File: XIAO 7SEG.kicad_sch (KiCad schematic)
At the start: 8 parts, among them J2 Conn_01x07, J4 Conn_01x07, Q1 AO3400A, Q2 AO3400A, U1 GS2816CW-G, U2 GS2816CW-G

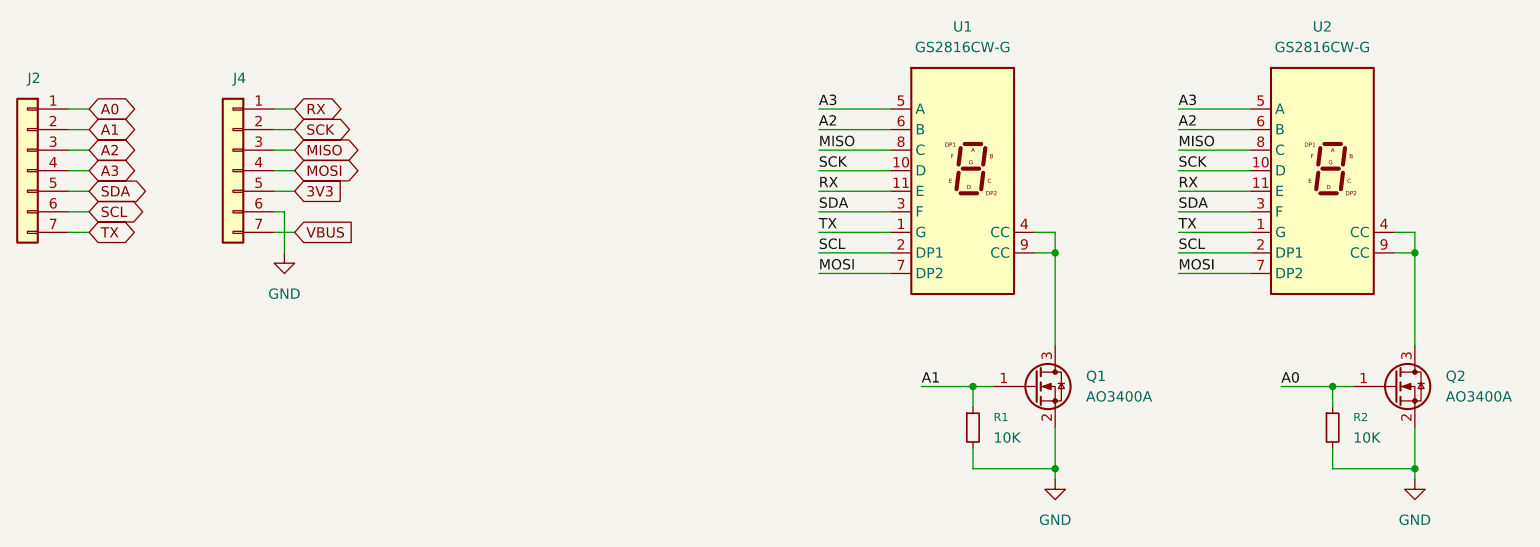
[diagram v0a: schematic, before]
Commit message: V2: Add series resistors
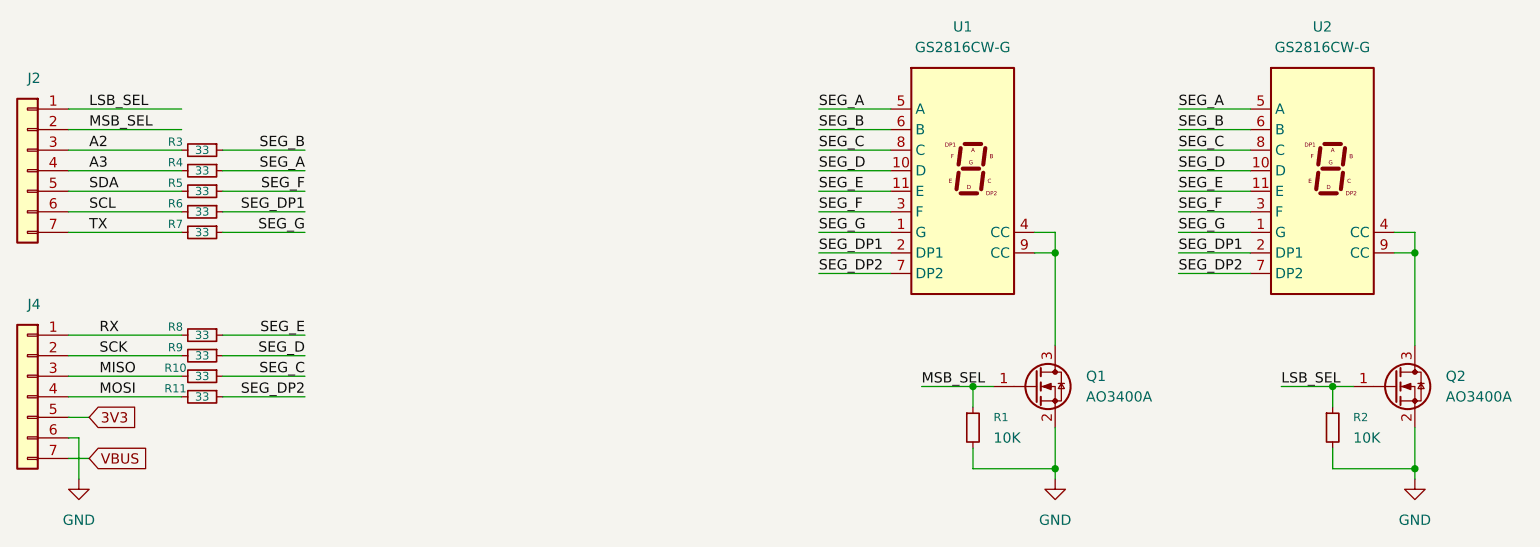
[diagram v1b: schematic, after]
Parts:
- added R10, R11, R3, R4, R5, R6, R7, R8, R9: 33, Resistor_SMD:R_0402_1005Metric, symbol Device:R_Small
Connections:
- net A2: now also R3.2; no longer U1.6 (B), U2.6 (B)
- net A3: now also R4.2; no longer U1.5 (A), U2.5 (A)
- net MISO: now also R10.2; no longer U1.8 (C), U2.8 (C)
- net MOSI: now also R11.2; no longer U1.7 (DP2), U2.7 (DP2)
- net RX: now also R8.2; no longer U1.11 (E), U2.11 (E)
- net SCK: now also R9.2; no longer U1.10 (D), U2.10 (D)
- net SCL: now also R6.2; no longer U1.2 (DP1), U2.2 (DP1)
- net SDA: now also R5.2; no longer U1.3 (F), U2.3 (F)
- net TX: now also R7.2; no longer U1.1 (G), U2.1 (G)
- net A0 renamed LSB_SEL
- net A1 renamed MSB_SEL
- new net SEG_A: R4.1, U1.5 (A), U2.5 (A)
- new net SEG_B: R3.1, U1.6 (B), U2.6 (B)
- new net SEG_C: R10.1, U1.8 (C), U2.8 (C)
- new net SEG_D: R9.1, U1.10 (D), U2.10 (D)
- new net SEG_DP1: R6.1, U1.2 (DP1), U2.2 (DP1)
- new net SEG_DP2: R11.1, U1.7 (DP2), U2.7 (DP2)
- new net SEG_E: R8.1, U1.11 (E), U2.11 (E)
- new net SEG_F: R5.1, U1.3 (F), U2.3 (F)
- new net SEG_G: R7.1, U1.1 (G), U2.1 (G)
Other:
- moved on the sheet: J4

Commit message: Renumber pins to make easier
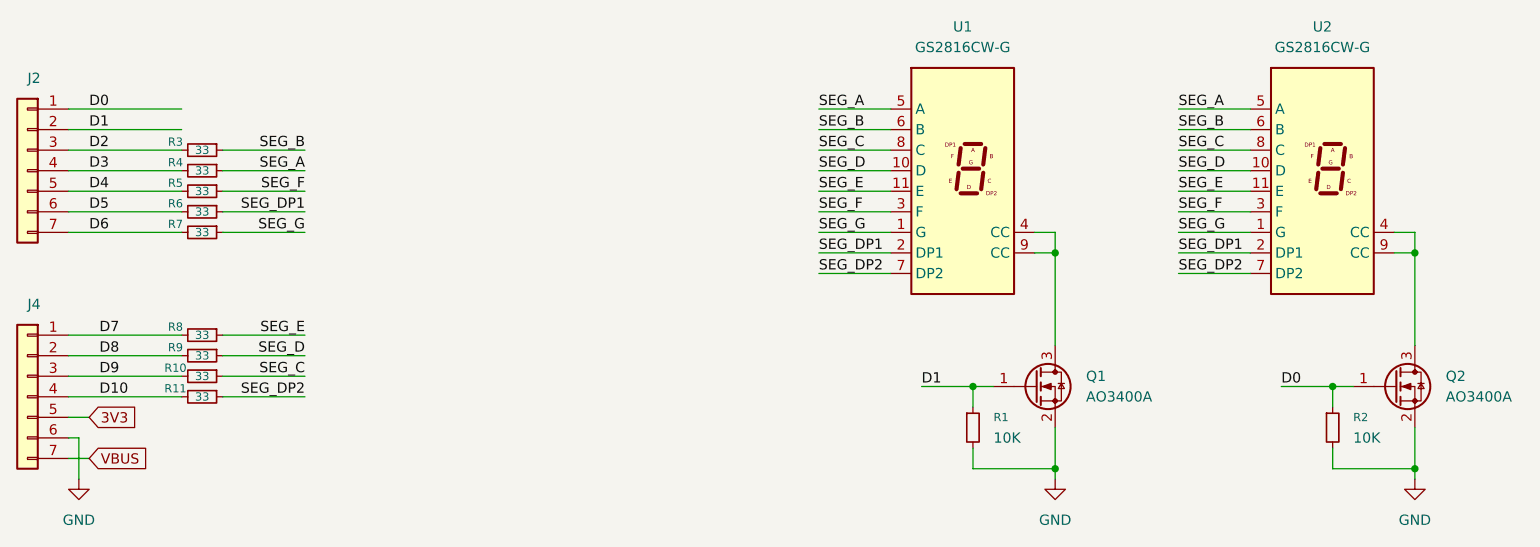
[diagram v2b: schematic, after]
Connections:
- net A2 renamed D2
- net A3 renamed D3
- net LSB_SEL renamed D0
- net MISO renamed D9
- net MOSI renamed D10
- net MSB_SEL renamed D1
- net RX renamed D7
- net SCK renamed D8
- net SCL renamed D5
- net SDA renamed D4
- net TX renamed D6
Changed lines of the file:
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@@
 		)
 	)
-	(label "SCK"
+	(label "D8"
 		(at 69.85 97.79 0)
 		(effects
@@
 		)
 	)
-	(label "TX"
+	(label "D6"
 		(at 68.58 82.55 0)
 		(effects
@@
 		)
 	)
-	(label "RX"
+	(label "D7"
 		(at 69.85 95.25 0)
 		(effects
@@
 		)
 	)
-	(label "MISO"
+	(label "D9"
 		(at 69.85 100.33 0)
 		(effects
@@
 		)
 	)
-	(label "LSB_SEL"
+	(label "D0"
 		(at 215.9 101.6 0)
 		(effects
@@
 		)
 	)
-	(label "A3"
+	(label "D3"
 		(at 68.58 74.93 0)
 		(effects
@@
 		)
 	)
-	(label "MOSI"
+	(label "D10"
 		(at 69.85 102.87 0)
 		(effects
@@
 		)
 	)
-	(label "SDA"
+	(label "D4"
 		(at 68.58 77.47 0)
 		(effects
@@
 		)
 	)
-	(label "LSB_SEL"
+	(label "D0"
 		(at 68.58 67.31 0)
 		(effects
@@
 		)
 	)
-	(label "MSB_SEL"
+	(label "D1"
 		(at 68.58 69.85 0)
 		(effects
@@
 		)
 	)
-	(label "MSB_SEL"
+	(label "D1"
 		(at 171.45 101.6 0)
 		(effects
@@
 		)
 	)
-	(label "SCL"
+	(label "D5"
 		(at 68.58 80.01 0)
 		(effects
@@
 		)
 	)
-	(label "A2"
+	(label "D2"
 		(at 68.58 72.39 0)
 		(effects
